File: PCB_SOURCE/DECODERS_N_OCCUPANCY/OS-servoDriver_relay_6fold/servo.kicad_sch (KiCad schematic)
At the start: 11 parts, among them J701 Conn_02x03_Odd_Even, K701 G6K-2F-Y-TR DC5, K702 G6K-2F-Y-TR DC5, Q701 NPN_TOR, Q702 NPN_TOR

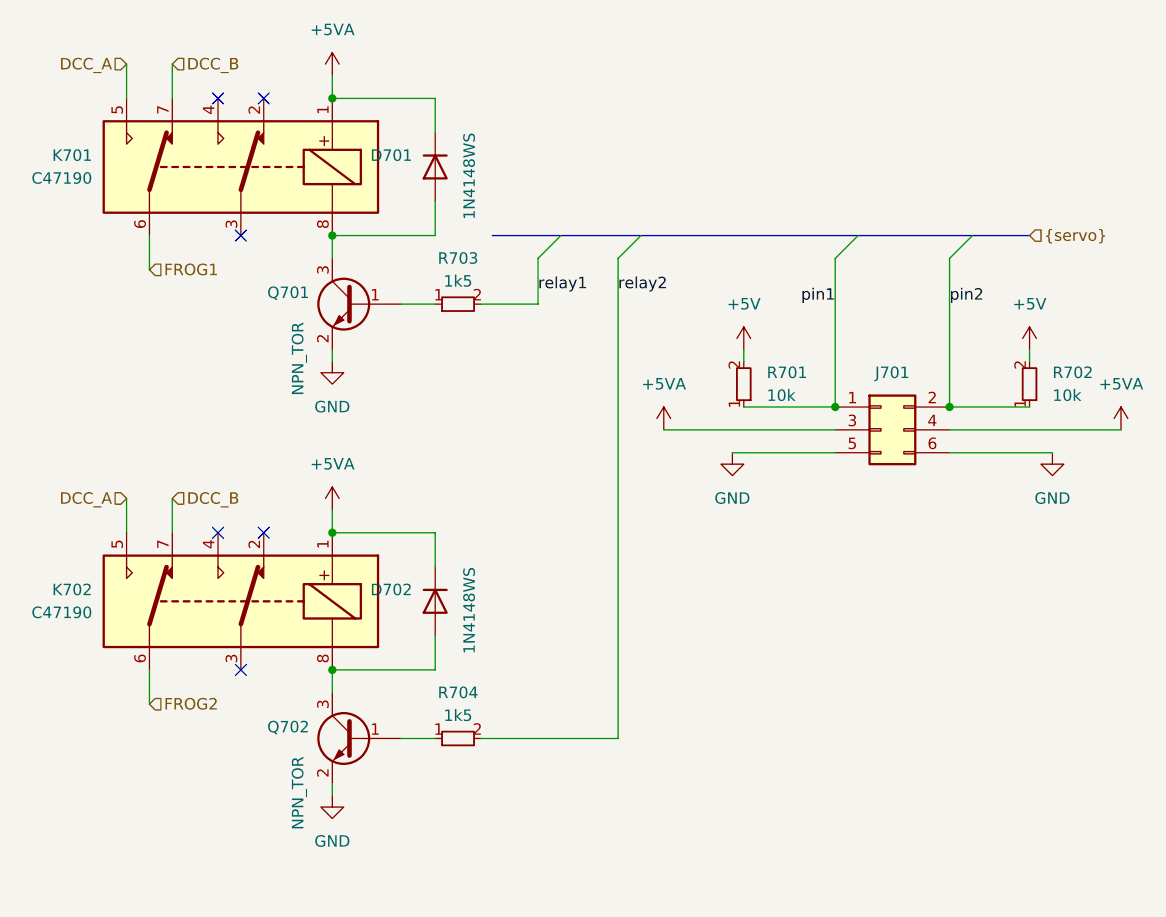
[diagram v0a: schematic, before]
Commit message: added S88 current sense to releases and update OSSD decoder
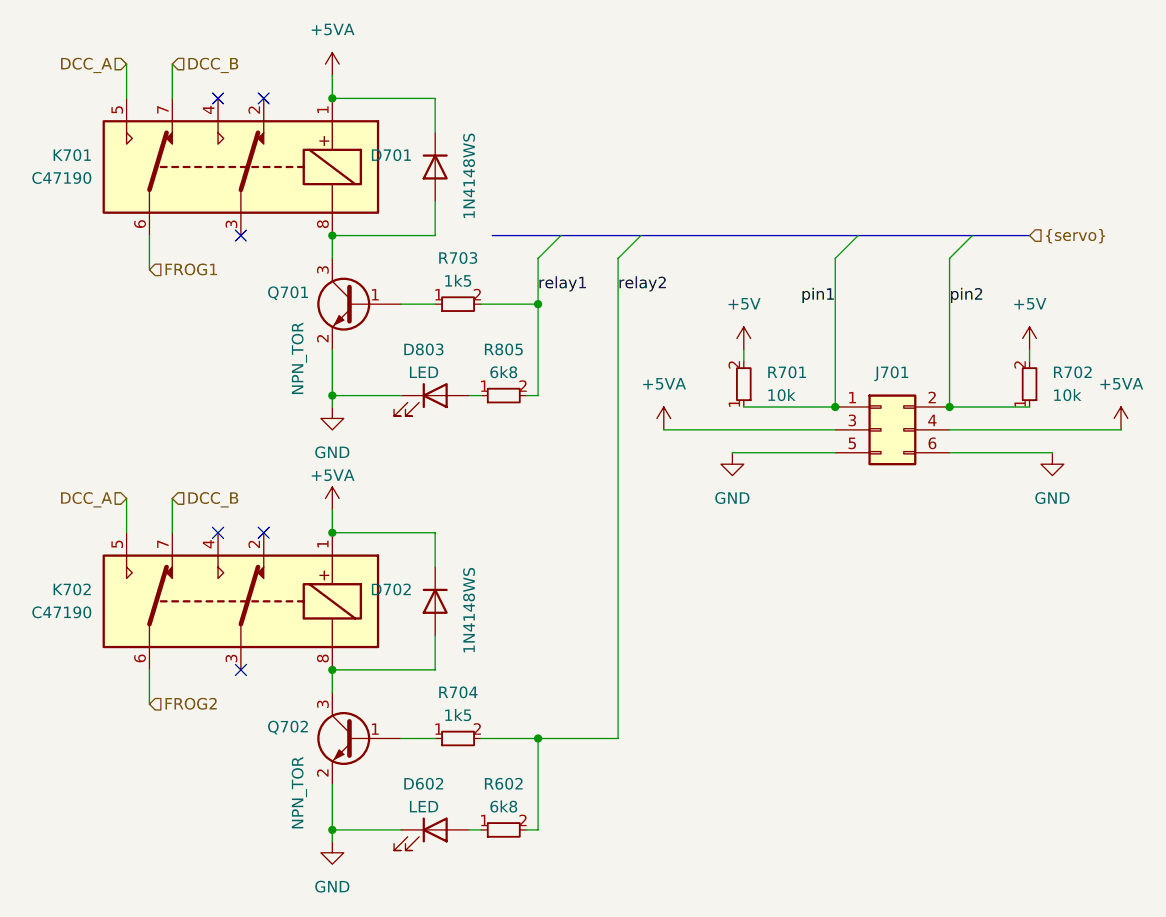
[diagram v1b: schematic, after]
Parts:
- added D602, D803: LED, LED_SMD:LED_0805_2012Metric_Pad1.15x1.40mm_HandSolder, symbol custom_kicad_lib_sk:LED
- added R602, R805: 6k8, custom_kicad_lib_sk:R_0603_smalltext, symbol resistors_0603:R_6k8_0603
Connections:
- net GND: now also D602.1 (K), D803.1 (K)
- net relay1: now also R805.2
- net relay2: now also R602.2
- new net: D602.2 (A), R602.1
- new net: D803.2 (A), R805.1
